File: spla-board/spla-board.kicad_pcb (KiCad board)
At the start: 4 copper layers, 178 x 107 mm, 238 parts, among them J1 USB_B_Micro, J12 J_POWER, J13 J_ANALOG, J14 J_AREF, J15 J_DPULL, J2 J_JTAG, J3 J_BODGE, J4 J_POWER2, J5 J_PPURESET, J6 J_SAMPLE, J7 Barrel_Jack, J8 J_AREF_AMP, U1 LFE5U-45F-BG256, U10 SNES_PPU1, U11 SNES_PPU2, U12 VRAM, U13 VRAM, U14 TLV73311PDBV, U15 74LVC8T245, U16 74LVC8T245, U17 74LVC8T245, U2 FT2232H, U20 74LVC8T245, U22 74LVC8T245, U23 74LVC8T245, U24 74LVC8T245, U25 74LVC8T245, U26 74LVC8T245, U27 74LVC8T245, U28 74LVC8T245, U29 74LVC8T245, U3 93LC66B, U30 74LVC8T245, U31 74LVC8T245, U32 74LVC8T245, U51 ADC1173, U52 ADC1173, U53 ADC1173, U61 LMH6611, U62 LMH6611, U63 LMH6611, U7 ST1S10PHR, U74 LMH6611, U75 LMH6611, U76 TLV73333PDBV, U8 ST1S10PHR, U9 TLV73325PDBV, X1 FT5HNBPK12.0-T1

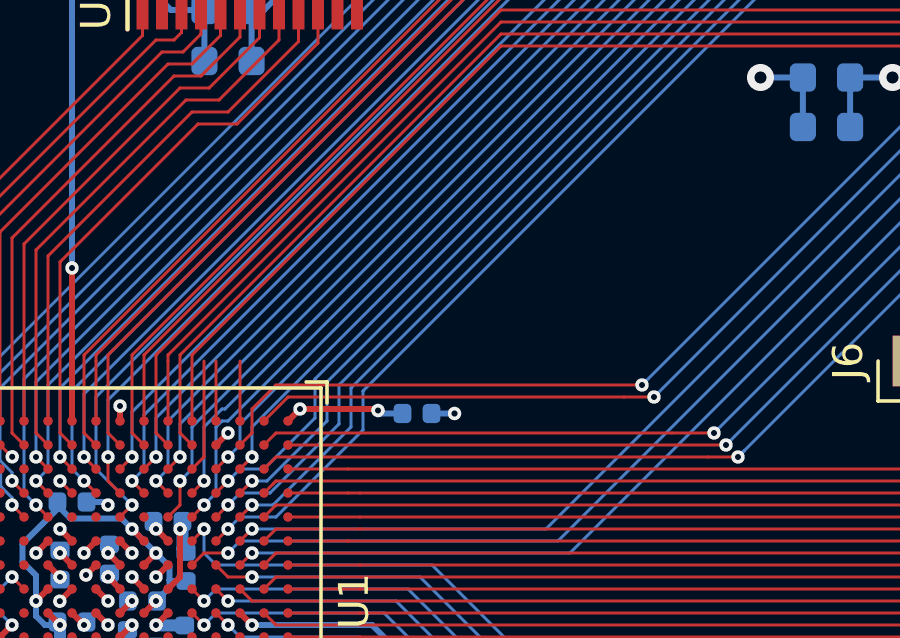
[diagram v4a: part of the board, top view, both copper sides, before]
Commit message: schematic/pcb: Add test points for remaining three FPGA pins.
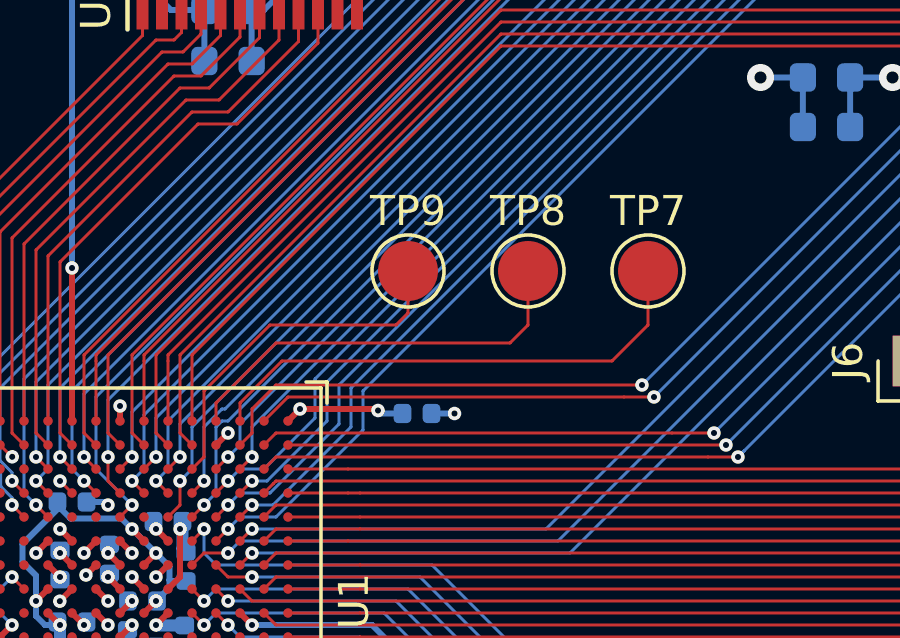
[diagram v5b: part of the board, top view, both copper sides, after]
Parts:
- added TP7: TestPoint, TestPoint:TestPoint_Pad_D2.0mm, F.Cu at (115.0, 89.0)
- added TP8: TestPoint, TestPoint:TestPoint_Pad_D2.0mm, F.Cu at (111.0, 89.0)
- added TP9: TestPoint, TestPoint:TestPoint_Pad_D2.0mm, F.Cu at (107.0, 89.0)
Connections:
- U1 pad C1: Net-(U1-PadC1) -> FPGA_EXTRA1
- U1 pad D1: Net-(U1-PadD1) -> FPGA_EXTRA2
- U1 pad E3: Net-(U1-PadE3) -> FPGA_EXTRA3
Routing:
- net FPGA_EXTRA1: track 0.00 -> 17.1 mm
- net FPGA_EXTRA2: track 0.00 -> 13.9 mm
- net FPGA_EXTRA3: track 0.00 -> 12.0 mm
- net Net-(U1-PadE3): track 3.77 -> 0.00 mm
- net Net-(U1-PadD1): track 2.00 -> 0.00 mm
- net Net-(U1-PadC1): track 2.00 -> 0.00 mm

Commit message: schematic/pcb: Add BoM-only symbols.
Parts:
- added BOM1: USB Cable, SPLA:BoM, F.Cu at (27.0, 116.0)
- added BOM10: Jumper, SPLA:BoM, F.Cu at (74.0, 177.0)
- added BOM11: Jumper, SPLA:BoM, F.Cu at (80.0, 177.0)
- added BOM12: Jumper, SPLA:BoM, F.Cu at (26.0, 184.0)
- added BOM13: Jumper, SPLA:BoM, F.Cu at (32.0, 184.0)
- added BOM14: Jumper, SPLA:BoM, F.Cu at (38.0, 184.0)
- added BOM15: Jumper, SPLA:BoM, F.Cu at (44.0, 184.0)
- added BOM16: Jumper, SPLA:BoM, F.Cu at (50.0, 184.0)
- added BOM17: Hex Standoff Male, SPLA:BoM, F.Cu at (96.0, 169.0)
- added BOM18: Hex Standoff Male, SPLA:BoM, F.Cu at (96.0, 176.0)
- added BOM19: Hex Standoff Male, SPLA:BoM, F.Cu at (96.0, 183.0)
- added BOM2: Jumper, SPLA:BoM, F.Cu at (26.0, 177.0)
- added BOM20: Hex Standoff Male, SPLA:BoM, F.Cu at (96.0, 191.0)
- added BOM21: Hex Standoff Female, SPLA:BoM, F.Cu at (114.0, 169.0)
- added BOM22: Hex Standoff Female, SPLA:BoM, F.Cu at (114.0, 176.0)
- added BOM23: Hex Standoff Female, SPLA:BoM, F.Cu at (114.0, 183.0)
- added BOM24: Hex Standoff Female, SPLA:BoM, F.Cu at (114.0, 190.0)
- added BOM25: Jumper, SPLA:BoM, F.Cu at (56.0, 184.0)
- added BOM26: Jumper, SPLA:BoM, F.Cu at (62.0, 184.0)
- added BOM3: Jumper, SPLA:BoM, F.Cu at (32.0, 177.0)
- added BOM4: Jumper, SPLA:BoM, F.Cu at (38.0, 177.0)
- added BOM5: Jumper, SPLA:BoM, F.Cu at (44.0, 177.0)
- added BOM6: Jumper, SPLA:BoM, F.Cu at (50.0, 177.0)
- added BOM7: Jumper, SPLA:BoM, F.Cu at (56.0, 177.0)
- added BOM8: Jumper, SPLA:BoM, F.Cu at (62.0, 177.0)
- added BOM9: Jumper, SPLA:BoM, F.Cu at (68.0, 177.0)

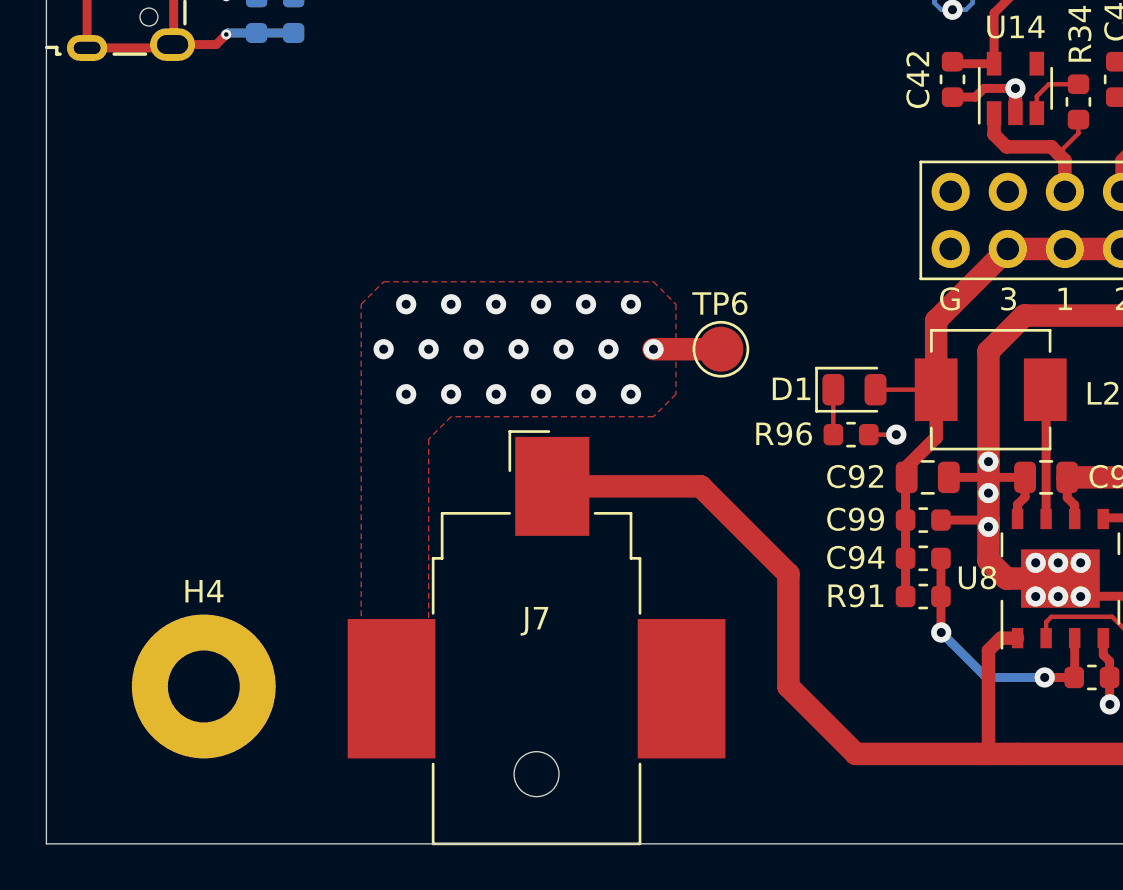
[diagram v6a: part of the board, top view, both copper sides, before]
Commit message: schematic/pcb: Add footprints for large input capacitors, NOSTUFF for now.
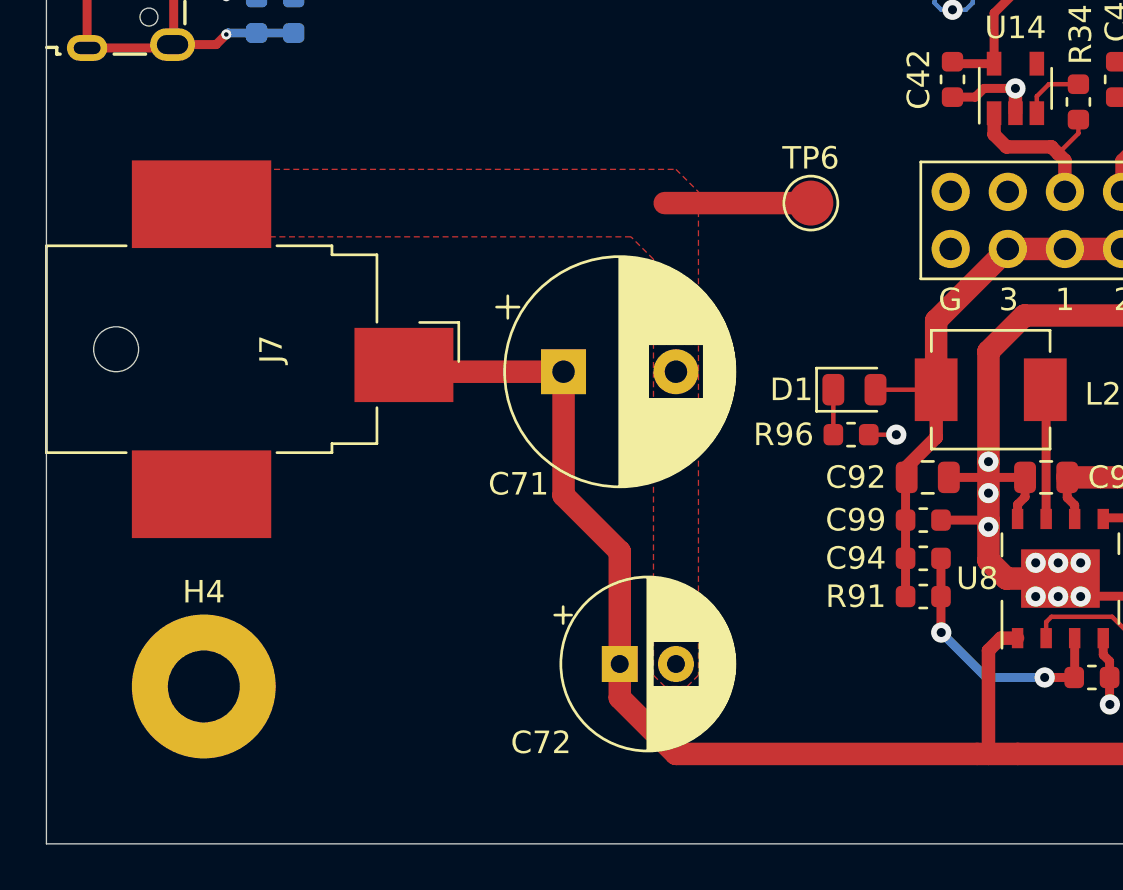
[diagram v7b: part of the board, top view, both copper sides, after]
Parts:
- added C71: NOSTUFF, Capacitor_THT:CP_Radial_D10.0mm_P5.00mm, F.Cu at (63.0, 134.0)
- added C72: NOSTUFF, Capacitor_THT:CP_Radial_D7.5mm_P2.50mm, F.Cu at (65.5, 147.0)
- TP7: value TestPoint -> TP_EXTRA1
- TP8: value TestPoint -> TP_EXTRA2
- TP9: value TestPoint -> TP_EXTRA3
- moved J7 16.7 mm to (50.1, 133.0), turned to 270 degrees
- moved TP6 7.63 mm to (74.0, 126.5)
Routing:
- net +12V: track 125.6 -> 138.7 mm
- net GND: track 488.7 -> 492.2 mm, vias 181 -> 162

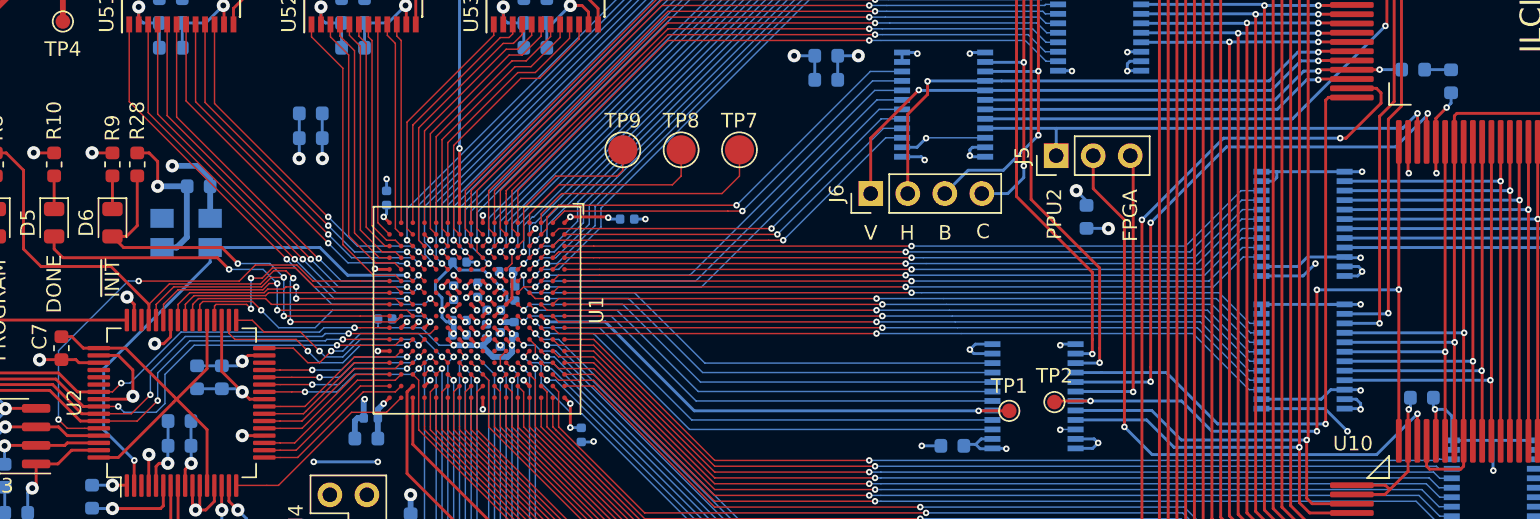
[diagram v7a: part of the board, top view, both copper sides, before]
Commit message: schematic/pcb: Add pullup to SPI_CS and pulldown to PPU2_RESET.
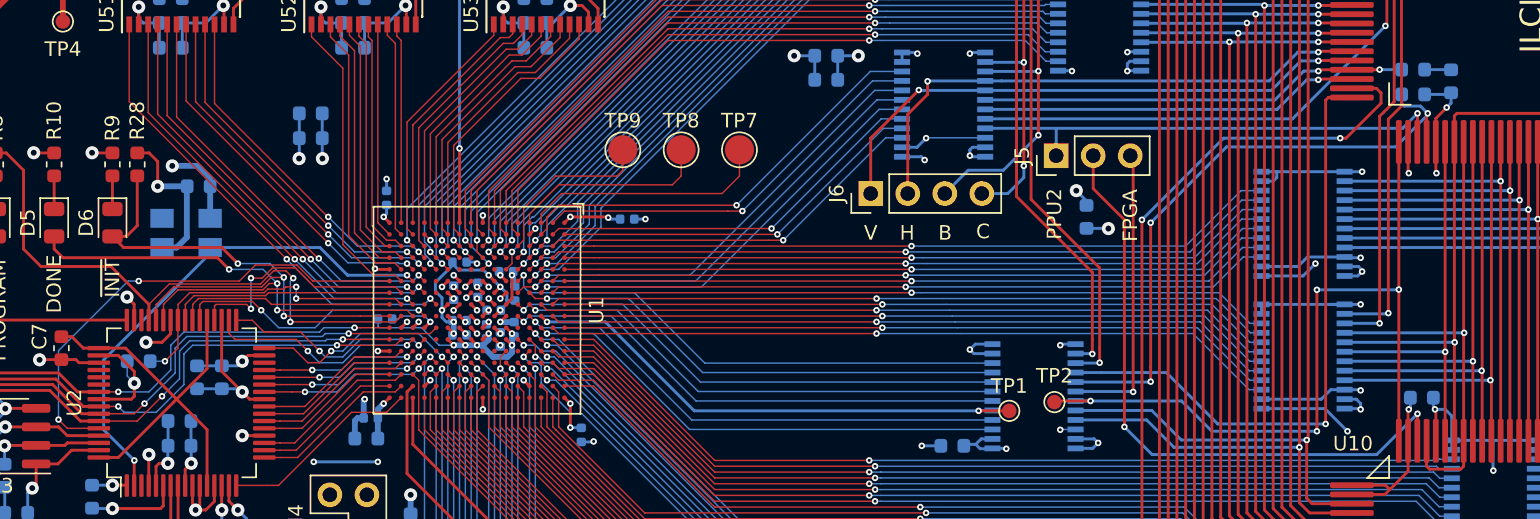
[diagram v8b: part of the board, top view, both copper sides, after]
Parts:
- added R29: 10k, Resistor_SMD:R_0603_1608Metric, B.Cu at (161.2, 85.2)
- added R30: 10k, Resistor_SMD:R_0603_1608Metric, B.Cu at (73.8, 103.5)
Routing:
- net SPI_~CS~: track 18.5 -> 22.7 mm, vias 2 -> 3
- net TAP_PPU2_~RESET~: track 40.2 -> 42.9 mm
- net +3V3: track 173.3 -> 175.5 mm
- net GND: track 492.2 -> 494.1 mm
- net JTAG_TCK: track 42.6 -> 43.6 mm
